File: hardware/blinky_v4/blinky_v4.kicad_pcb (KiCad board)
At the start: 2 copper layers, 120 x 70 mm, 207 parts, among them J1 RJ45, J10 Conn_01x04, J11 Conn_01x08, J2 Conn_01x06_Pin, J3 Conn_01x05_Pin, J4 Conn_01x07, J5 Conn_01x06_Pin, J6 Conn_01x04_Pin, J7 Conn_01x04_Pin, J8 Conn_01x03_Pin, J9 Conn_02x10_Odd_Even, Q1 2N7002, Q2 2N7002, Q3 2N7002, Q4 2N7002, Q5 2N7002, Q6 2N7002, Q7 2N7002, Q8 2N7002, U1 ADA4807-1, U10 STM32F405RGTx, U11 AMS1117-3.3, U12 BA50DD0WHFP-TR, U2 SN74LVC1G14DBV, U3 SN74LVC1G14DBV, U4 ADA4807-1, U5 ADA4807-1, U6 TLV3603DCKR, U7 SN74LVC1G14DBV, U8 TLV3603DCKR, U9 L78L05_SOT89, Y1 AOCJY4A-10.000MHZ-SW, Y2 16MHz

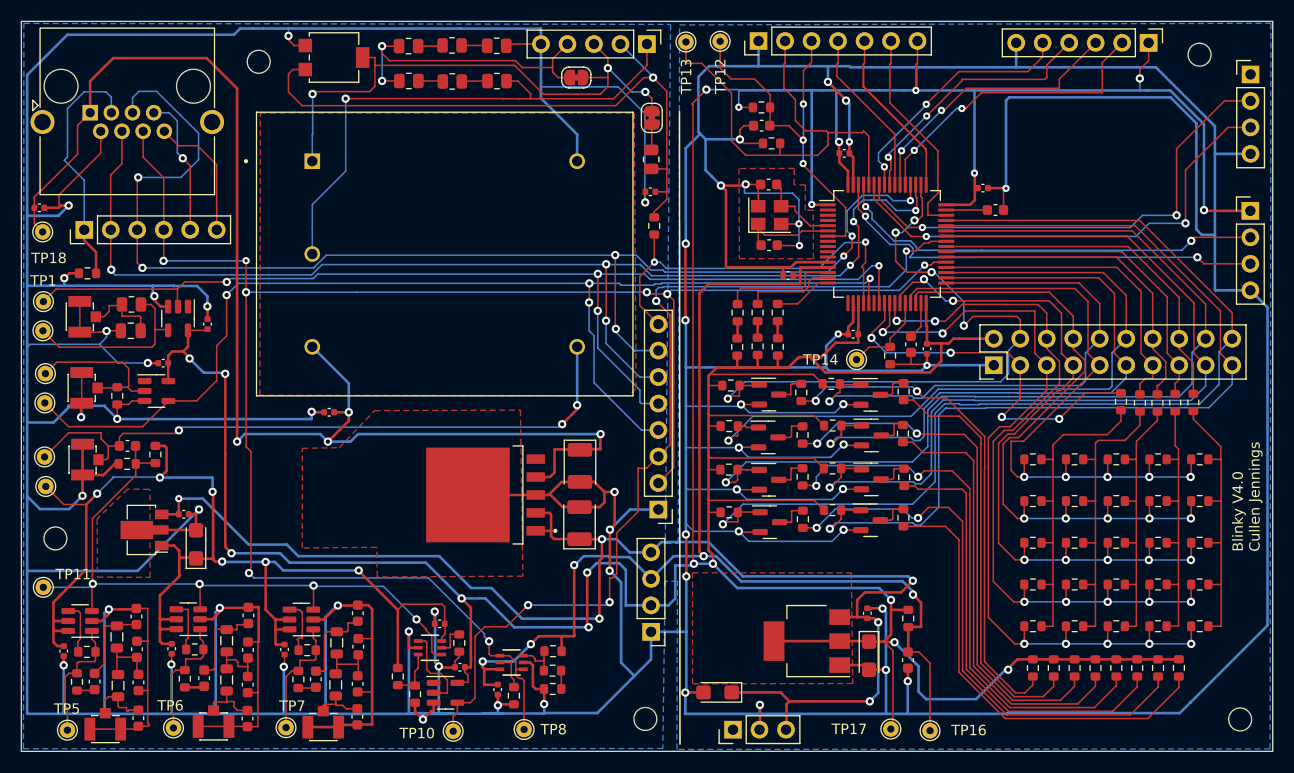
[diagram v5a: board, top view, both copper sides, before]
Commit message: added JST connectors
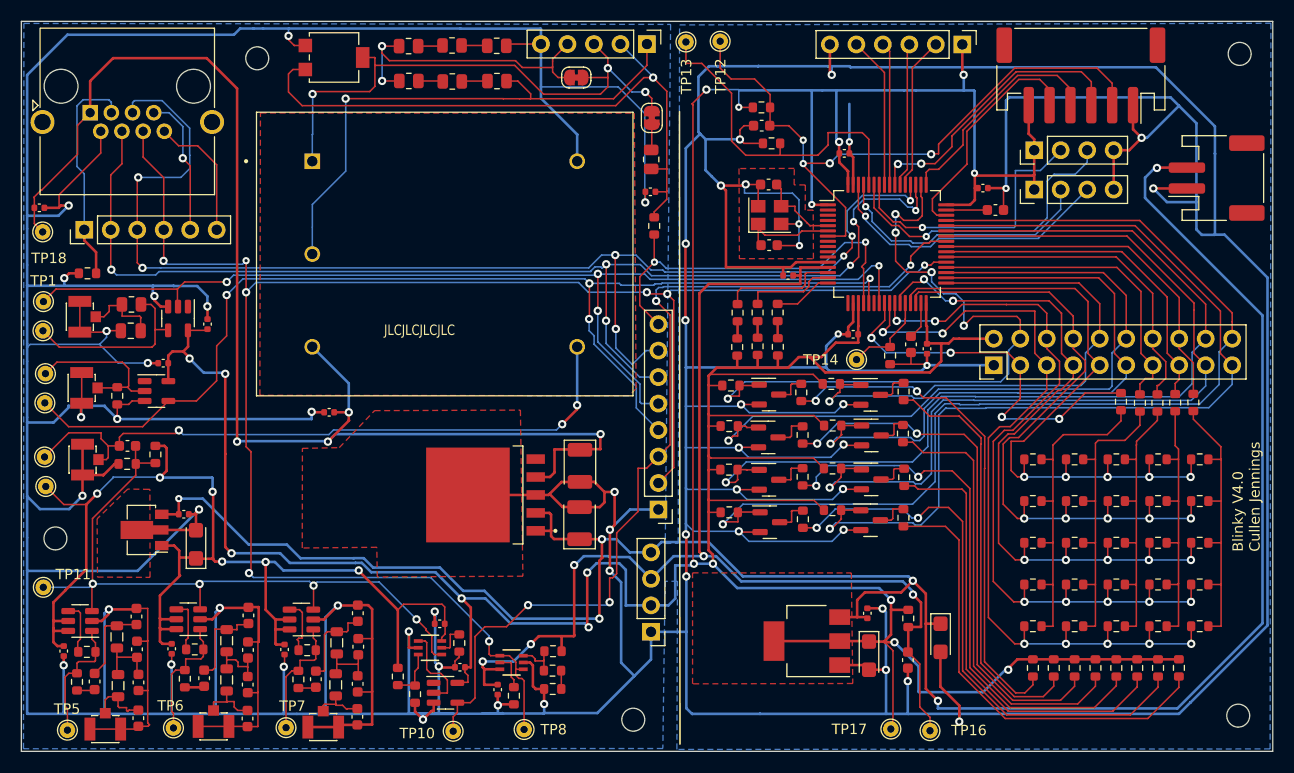
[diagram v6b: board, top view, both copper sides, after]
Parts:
- removed J4: Conn_01x07, Connector_PinHeader_2.54mm:PinHeader_1x07_P2.54mm_Vertical
- added J12: Conn_01x06, Connector_JST:JST_PH_S6B-PH-SM4-TB_1x06-1MP_P2.00mm_Horizontal, F.Cu at (201.6, 55.2)
- J8: value Conn_01x03_Pin -> Conn_01x02; footprint Connector_PinHeader_2.54mm:PinHeader_1x03_P2.54mm_Vertical -> Connector_JST:JST_PH_S2B-PH-SM4-TB_1x02-1MP_P2.00mm_Horizontal
- moved J8 70.3 mm to (214.6, 65.0)
- moved C43 22.0 mm to (188.1, 109.1), turned to -90 degrees
- moved J6 22.0 mm to (197.1, 62.4), turned to 90 degrees
- moved J7 20.8 mm to (197.1, 66.1), turned to 90 degrees
- moved J5 17.9 mm to (190.2, 52.2)
- moved H2 3.85 mm to (216.8, 53.1)
- moved H3 1.16 mm to (158.7, 117.0)
- moved H4 0.41 mm to (216.7, 116.6)
- moved H1 0.36 mm to (122.6, 53.5)
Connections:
- J8 pad 1: unconnected-(J8-Pin_1-Pad1) -> GND
- J8 pad 2: GND -> +6V
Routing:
- net +6V: track 133.8 -> 209.6 mm
- net +3.3V: track 454.9 -> 427.1 mm, vias 19 -> 17
- net /NRST: track 37.6 -> 64.4 mm, vias 3 -> 4
- net /USB_RX: track 46.9 -> 26.6 mm, vias 2 -> 1
- net /USB_TX: track 46.3 -> 30.0 mm, vias 2 -> 1
- net GND: track 1073.6 -> 1089.7 mm
- net /SCL: track 41.8 -> 26.0 mm, vias 2 -> 1
- net /SDA: track 43.2 -> 28.3 mm, vias 2 -> 1
- net /DB4: track 29.5 -> 14.7 mm, vias 2 -> 0
- net /DB3: track 26.7 -> 13.8 mm, vias 2 -> 0
- net /BOOT0: track 45.3 -> 33.3 mm
- net /DB2: track 25.6 -> 13.7 mm, vias 2 -> 0
- net /SWDTRC: track 16.1 -> 27.6 mm, vias 0 -> 2
- net /DB1: track 24.2 -> 14.6 mm, vias 2 -> 0
- net /SWDCLK: track 16.3 -> 21.8 mm
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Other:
- board text added: "JLCJLCJLCJLC"

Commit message: add othe TXCO
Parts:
- added X1: GTXO-14V (2.048MHz), Oscillator:Oscillator_DIP-14, F.Cu at (139.6, 64.5)
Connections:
- RV1 pad 1: GND -> unconnected-(RV1-Pad1)
- RV1 pad 2: Net-(J3-Pin_3) -> unconnected-(RV1-Pad2)
- RV1 pad 3: Net-(J3-Pin_2) -> unconnected-(RV1-Pad3)
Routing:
- net +3.3VA: track 115.4 -> 180.0 mm, vias 5 -> 7
- net GND: track 1089.7 -> 1121.1 mm, vias 56 -> 57
- net Net-(J3-Pin_3): track 54.1 -> 66.3 mm
- net /OCXO_OUT: track 63.3 -> 69.9 mm
- net Net-(J3-Pin_2): track 61.7 -> 60.5 mm

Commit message: add othe TXCO
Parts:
- moved R17 0.56 mm to (145.0, 52.3)
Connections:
- J3 pad 5: GND -> +3.3VA
- RV1 pad 1: unconnected-(RV1-Pad1) -> GND
- RV1 pad 2: unconnected-(RV1-Pad2) -> Net-(J3-Pin_3)
- RV1 pad 3: unconnected-(RV1-Pad3) -> Net-(J3-Pin_2)
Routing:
- net +3.3VA: track 180.0 -> 204.0 mm
- net GND: track 1121.1 -> 1124.7 mm, vias 57 -> 58
- net Net-(J3-Pin_2): track 60.5 -> 61.7 mm
- net Net-(R14-Pad2): track 2.54 -> 1.91 mm
